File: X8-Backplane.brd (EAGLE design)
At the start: 122.1 x 122.1 mm, 17 parts

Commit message: Moved the board into a valid location
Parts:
- moved APPLICATION_BOARD 70.9 mm to (54.9, 44.5)
- moved BRICKS_COM 70.9 mm to (80.8, -16.3)
- moved BUCK_REGULATOR_BOARD 70.9 mm to (60.2, -9.40)
- moved ETH_POWER 70.9 mm to (96.5, 80.8)
- moved EXTRA_SERVO 70.9 mm to (103.6, 7.62)
- moved MAIN_CAM_DATA 70.9 mm to (80.8, 66.5)
- moved MAIN_CAM_POW 70.9 mm to (80.8, 78.5)
- moved MICRO_BOARD 70.9 mm to (59.2, 9.40)
- moved NAV_COM 70.9 mm to (57.9, 90.4)
- moved NAV_POWER 70.9 mm to (80.8, 90.4)
- moved POWER_INPUT 70.9 mm to (57.9, -16.3)
- moved SEC_CAM_1 70.9 mm to (57.9, 78.5)
- moved SEC_CAM_2 70.9 mm to (57.9, 66.5)
- moved SOLENOID_DATA 70.9 mm to (80.8, 7.62)
- moved SOLENOID_POWER 70.9 mm to (57.9, -4.32)
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
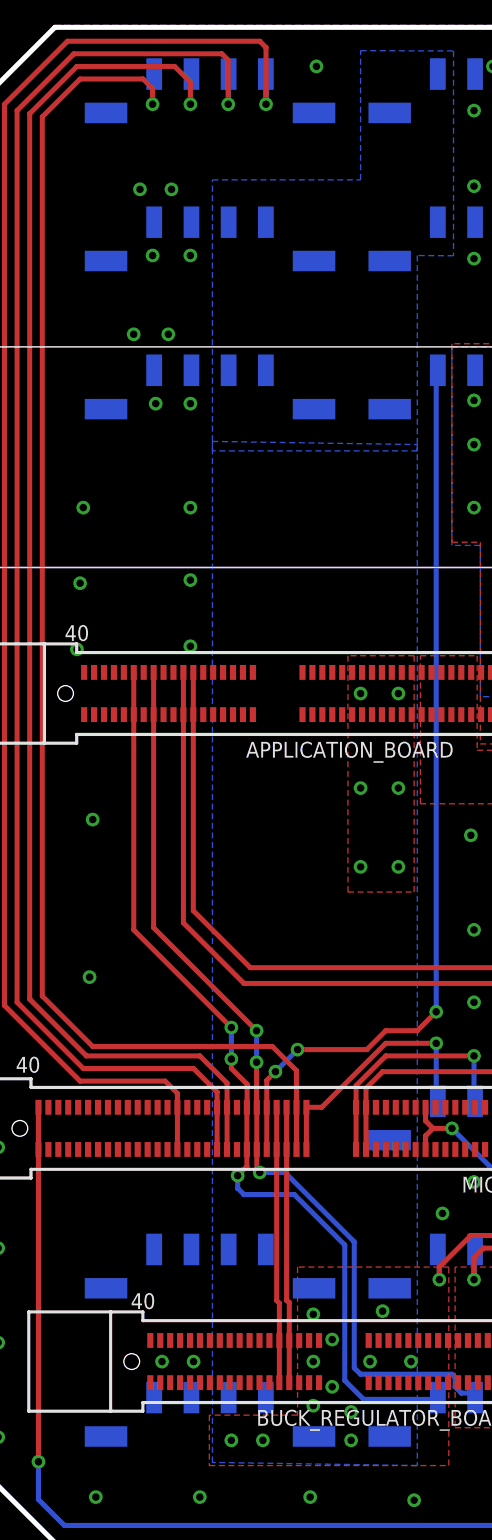
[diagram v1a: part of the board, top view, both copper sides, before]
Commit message: Made SCL and SDA lines of equal length
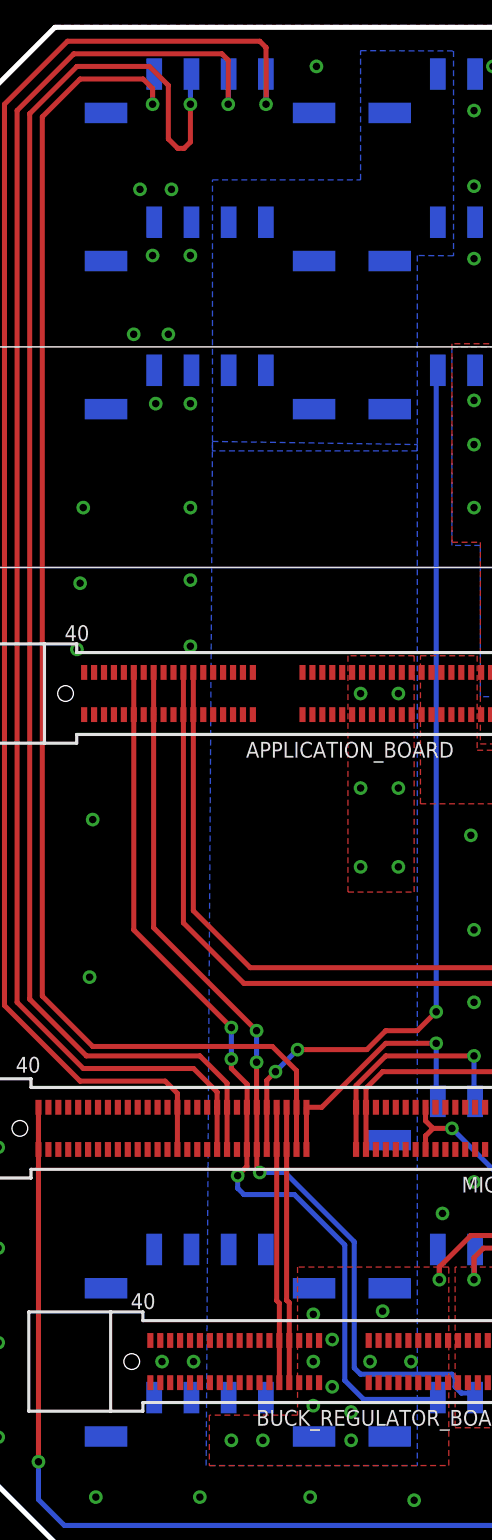
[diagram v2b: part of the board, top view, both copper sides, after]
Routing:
- net NAV_SDA: track 114.7 -> 121.0 mm
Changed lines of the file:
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@@
 </polygon>
 <polygon width="0.4064" layer="16" rank="2">
-<vertex x="48.006" y="-17.526"/>
+<vertex x="47.498" y="-17.78"/>
 <vertex x="48.006" y="64.77"/>
 <vertex x="64.516" y="64.516"/>
@@
 <contactref element="NAV_COM" pad="C3"/>
 <wire x1="49.182" y1="7.698" x2="49.182" y2="11.098" width="0.4064" layer="1"/>
-<wire x1="44.958" y1="94.996" x2="46.228" y2="93.726" width="0.4064" layer="1"/>
-<wire x1="46.228" y1="93.726" x2="46.228" y2="91.948" width="0.4064" layer="1"/>
 <via x="46.228" y="91.948" extent="1-16" drill="0.6"/>
-<wire x1="46.228" y1="91.948" x2="46.228" y2="94.295" width="0.4064" layer="16"/>
 <wire x1="46.228" y1="94.295" x2="46.312" y2="94.379" width="0.4064" layer="16"/>
 <wire x1="49.182" y1="11.098" x2="49.182" y2="13.048" width="0.4064" layer="1"/>
@@
 <wire x1="33.274" y1="19.812" x2="33.274" y2="91.186" width="0.4064" layer="1"/>
 <wire x1="33.274" y1="91.186" x2="37.084" y2="94.996" width="0.4064" layer="1"/>
-<wire x1="37.084" y1="94.996" x2="44.958" y2="94.996" width="0.4064" layer="1"/>
+<wire x1="37.084" y1="94.996" x2="42.926" y2="94.996" width="0.4064" layer="1"/>
+<wire x1="42.926" y1="94.996" x2="44.45" y2="93.472" width="0.4064" layer="1"/>
+<wire x1="44.45" y1="93.472" x2="44.45" y2="89.154" width="0.4064" layer="1"/>
+<wire x1="44.45" y1="89.154" x2="45.212" y2="88.392" width="0.4064" layer="1"/>
+<wire x1="45.212" y1="88.392" x2="45.72" y2="88.392" width="0.4064" layer="1"/>
+<wire x1="45.72" y1="88.392" x2="46.228" y2="88.9" width="0.4064" layer="1"/>
+<wire x1="46.228" y1="88.9" x2="46.228" y2="91.948" width="0.4064" layer="1"/>
+<wire x1="46.228" y1="94.295" x2="46.228" y2="91.948" width="0.4064" layer="16"/>
 </signal>
 <signal name="SONAR_PWM">
